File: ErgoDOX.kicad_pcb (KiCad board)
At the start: 2 copper layers, 182.8 x 158.9 mm, 113 parts, among them J1 USB, J2 3.5mm, J3 JMP, J4 JMP, J5 JMP, J6 JMP, SW1 SWITCH_PUSH, SW10 SWITCH_PUSH, SW11 SWITCH_PUSH, SW12 SWITCH_PUSH, SW13 SWITCH_PUSH, SW14 SWITCH_PUSH, SW15 SWITCH_PUSH, SW16 SWITCH_PUSH, SW17 SWITCH_PUSH, SW18 SWITCH_PUSH, SW19 SWITCH_PUSH, SW2 SWITCH_PUSH, SW20 SWITCH_PUSH, SW21 SWITCH_PUSH, SW22 SWITCH_PUSH, SW23 SWITCH_PUSH, SW24 SWITCH_PUSH, SW25 SWITCH_PUSH, SW26 SWITCH_PUSH, SW27 SWITCH_PUSH, SW28 SWITCH_PUSH, SW29 SWITCH_PUSH, SW3 SWITCH_PUSH, SW30 SWITCH_PUSH, SW31 SWITCH_PUSH, SW32 SWITCH_PUSH, SW33 SWITCH_PUSH, SW34 SWITCH_PUSH, SW35 SWITCH_PUSH, SW36 SWITCH_PUSH, SW37 SWITCH_PUSH, SW38 SWITCH_PUSH, SW39 SWITCH_PUSH, SW4 SWITCH_PUSH, SW40 SWITCH_PUSH, SW41 SWITCH_PUSH, SW42 SWITCH_PUSH, SW43 SWITCH_PUSH, SW44 SWITCH_PUSH, SW45 SWITCH_PUSH, SW46 SWITCH_PUSH, SW5 SWITCH_PUSH, SW6 SWITCH_PUSH, SW7 SWITCH_PUSH, SW8 SWITCH_PUSH, SW9 SWITCH_PUSH, U1 ProMicro

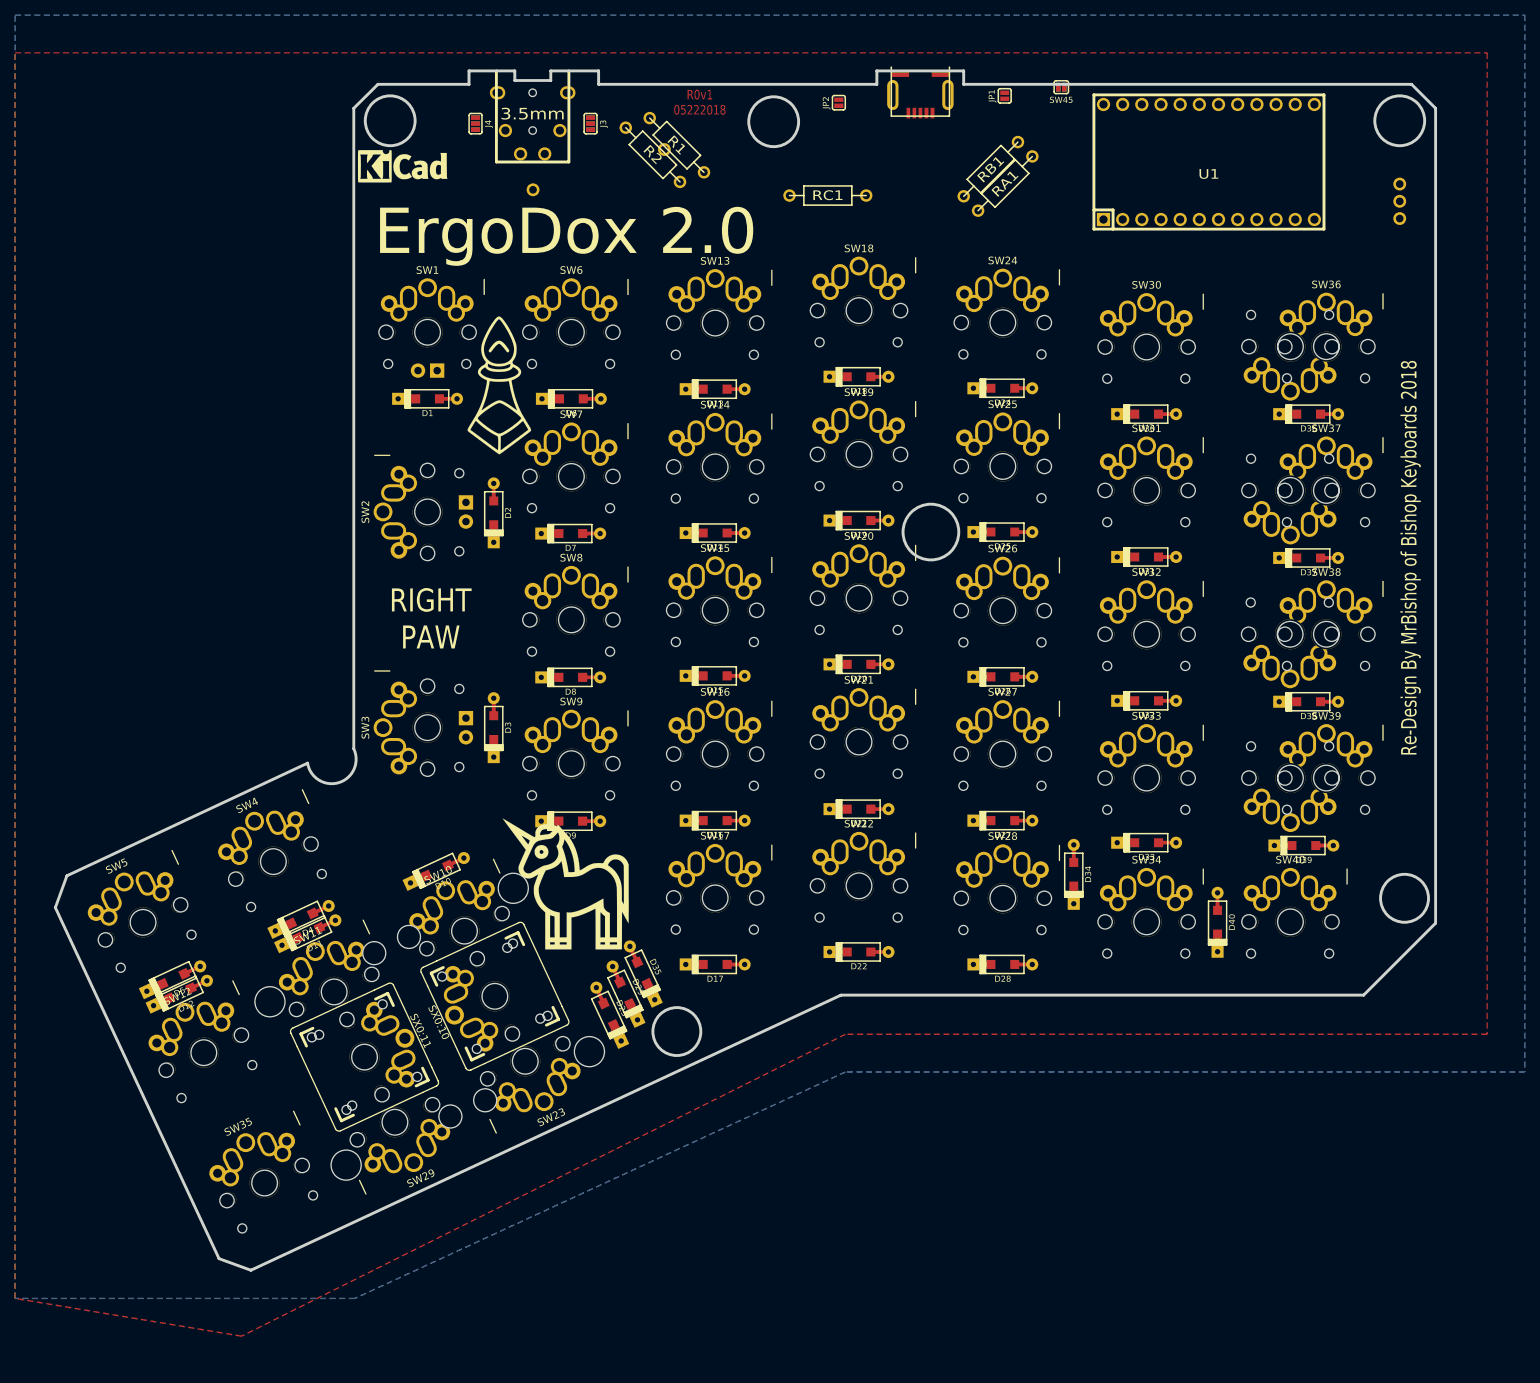
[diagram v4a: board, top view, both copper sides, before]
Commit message: fixed switch placement and begun traces
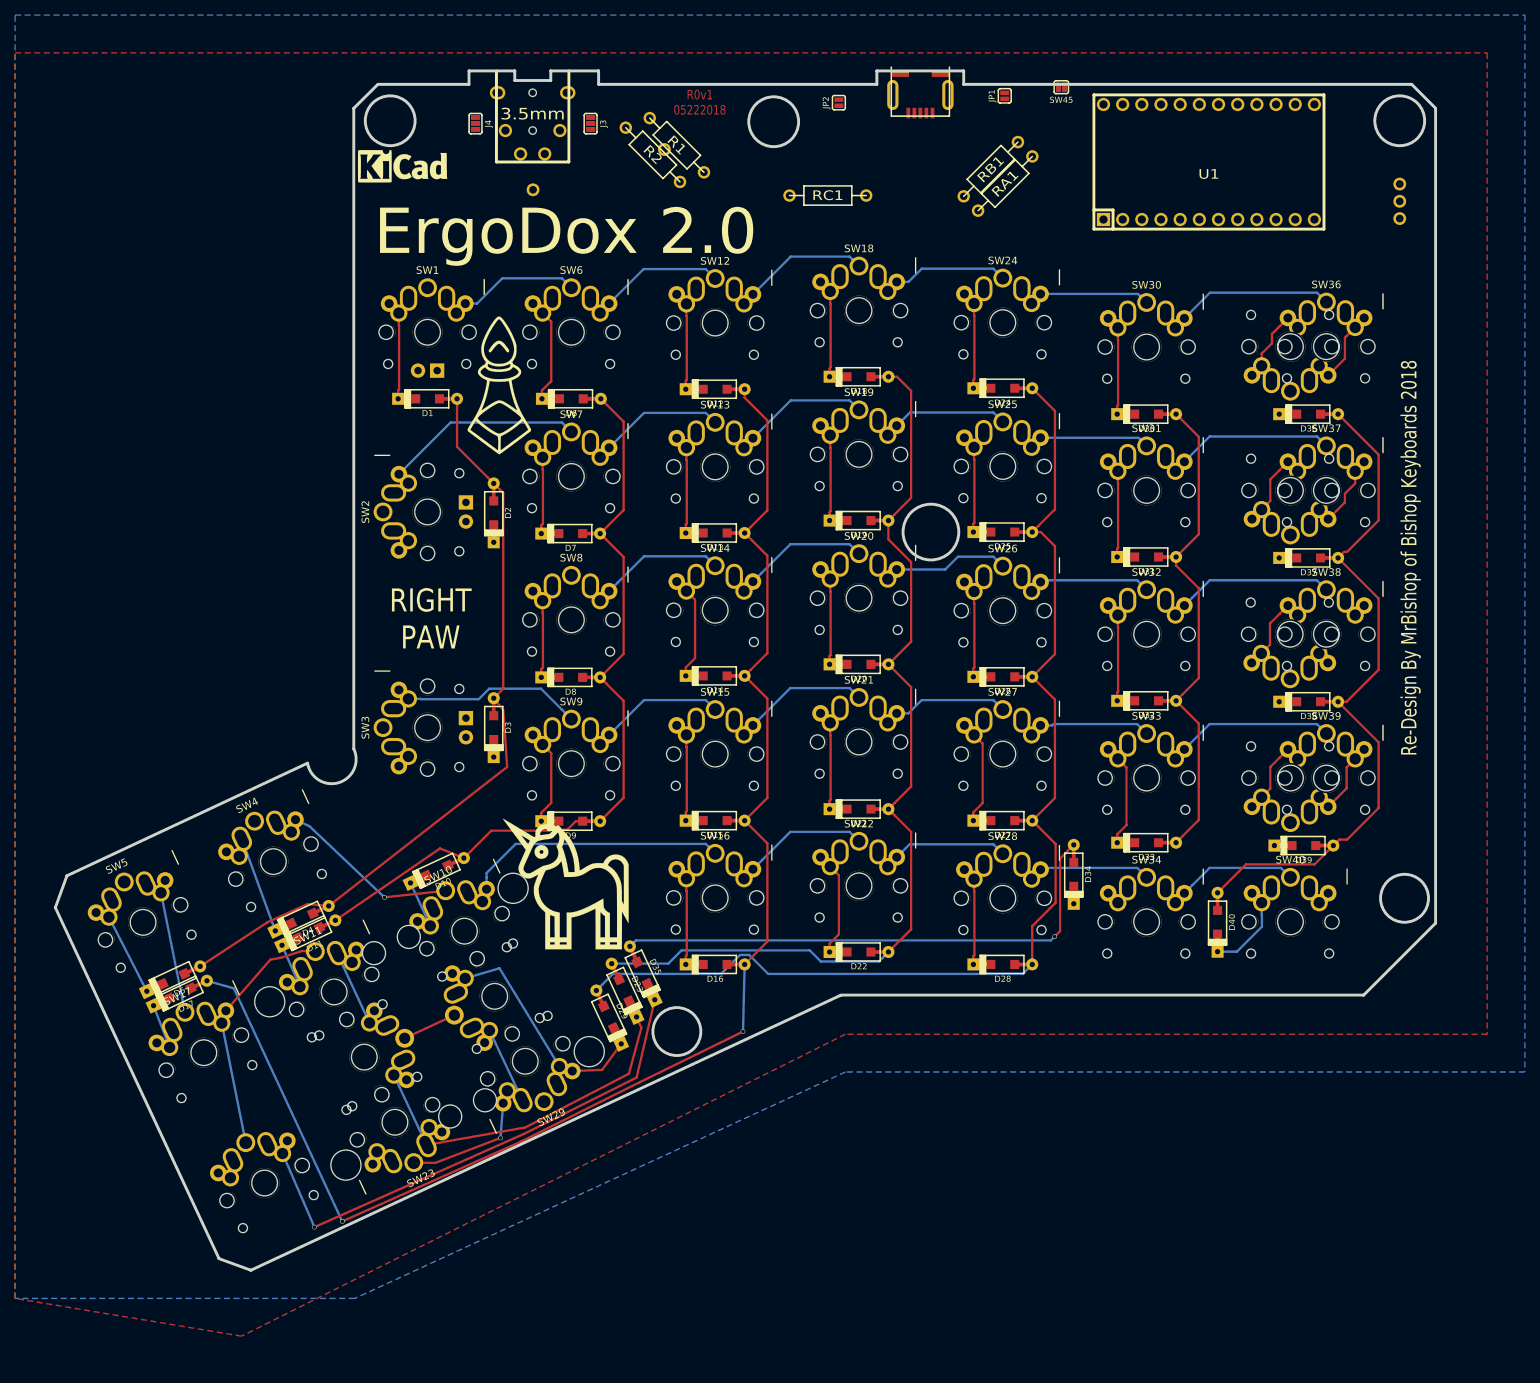
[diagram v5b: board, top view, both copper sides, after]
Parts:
- SW35: moved to B.Cu
- SX0:10: renamed from SX0:11; value SX0:2 -> SX0:3; moved to B.Cu
- SX0:11: renamed from SX0:10; value SX0:3 -> SX0:2; moved to B.Cu
- moved D29 3.84 mm to (96.4, 155.8)
- moved D23 3.77 mm to (98.4, 152.3)
- turned SX0:10 to 115 degrees
- turned SX0:11 to 295 degrees
- turned SW35 to 205 degrees
- renumbered D13 to D12, D14 to D13, D15 to D14, D16 to D15, D17 to D16, D12 to D17, SW13 to SW12, SW14 to SW13, SW15 to SW14, SW16 to SW15, SW17 to SW16, SW12 to SW17, SW29 to SW23, SW23 to SW29
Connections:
- SW12 pad 1: /ROW4 -> /ROW5
- SW13 pad 1: /ROW3 -> /ROW4
- SW14 pad 1: /ROW2 -> /ROW3
- SW15 pad 1: /ROW1 -> /ROW2
- SW16 pad 1: /ROW0 -> /ROW1
- SW17 pad 1: /ROW5 -> /ROW0
- SW23 pad 2: Net-(D29-Pad1) -> Net-(D23-Pad1)
- SW29 pad 2: Net-(D23-Pad1) -> Net-(D29-Pad1)
- SX0:10 pad 2: Net-(D29-Pad1) -> Net-(D23-Pad1)
- SX0:11 pad 2: Net-(D23-Pad1) -> Net-(D29-Pad1)
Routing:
- net /COL4: track 0.00 -> 191.6 mm, vias 0 -> 2
- net /COL2: track 0.00 -> 148.3 mm
- net /COL1: track 0.00 -> 134.2 mm, vias 0 -> 1
- net /COL3: track 0.00 -> 125.4 mm
- net /ROW1: track 0.00 -> 120.9 mm, vias 0 -> 1
- net /ROW4: track 0.00 -> 117.7 mm
- net /ROW2: track 0.00 -> 115.4 mm
- net /ROW5: track 0.00 -> 107.4 mm
- net /COL5: track 0.00 -> 101.6 mm
- net /COL6: track 0.00 -> 101.5 mm
- net /ROW0: track 0.00 -> 91.8 mm, vias 0 -> 1
- net /COL0: track 0.00 -> 90.1 mm
- net /ROW3: track 0.00 -> 83.8 mm
- net Net-(D35-Pad1): track 0.00 -> 68.3 mm, vias 0 -> 1
- net Net-(D23-Pad1): track 0.00 -> 46.8 mm
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
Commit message: initial traces complete
dont judge me on the thumb section i'm not crazy about how weird the wire traces are either.
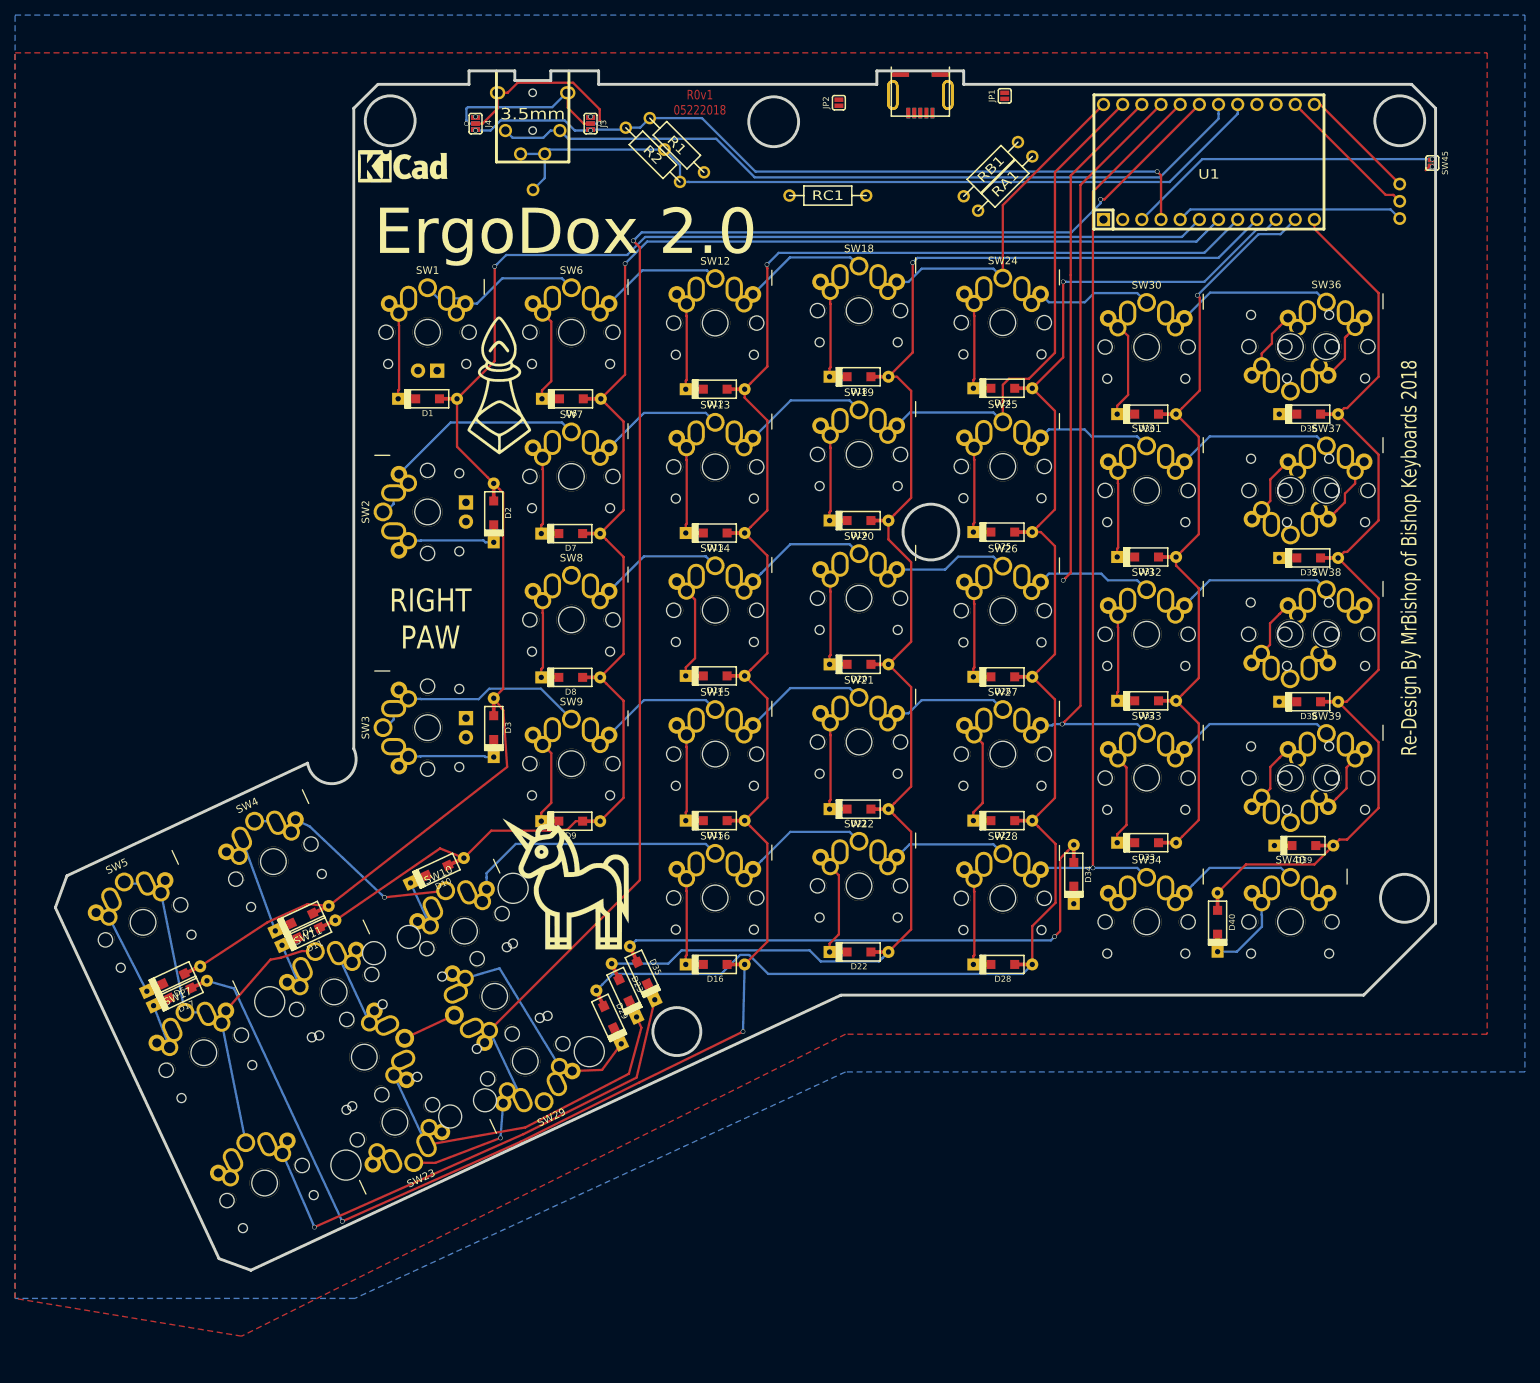
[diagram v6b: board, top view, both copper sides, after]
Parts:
- added J7: USB, BishopKicadConsolidated:USB_miniB_hirose_5S8, B.Cu at (137.7, 36.1)
- moved SW45 50.2 mm to (205.5, 42.7), turned to 270 degrees
- moved SW46 50.2 mm to (205.5, 42.7), turned to 270 degrees
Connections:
- J1 pad 2: (no net) -> /D-
- J1 pad 3: (no net) -> /D+
- J1 pad 4: (no net) -> /ID
- U1 pad 10: /COL4 -> /COL2
- U1 pad 11: /COL5 -> /COL1
- U1 pad 12: /COL6 -> /COL0
- U1 pad 6: /COL0 -> /COL6
- U1 pad 7: /COL1 -> /COL5
- U1 pad 8: /COL2 -> /COL4
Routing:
- net /ROW0: track 91.8 -> 302.4 mm, vias 1 -> 3
- net /COL6: track 101.5 -> 217.1 mm, vias 0 -> 1
- net /ROW1: track 120.9 -> 234.2 mm, vias 1 -> 2
- net /XTRADATA: track 0.00 -> 108.7 mm
- net /DATA: track 0.00 -> 102.9 mm
- net VCC: track 0.00 -> 101.7 mm, vias 0 -> 3
- net /COL5: track 101.6 -> 201.9 mm, vias 0 -> 1
- net /ROW2: track 115.4 -> 210.5 mm, vias 0 -> 1
- net /COL4: track 191.6 -> 274.2 mm, vias 2 -> 3
- net /ROW3: track 83.8 -> 151.8 mm, vias 0 -> 1
- net /COL3: track 125.4 -> 189.8 mm, vias 0 -> 1
- net /ROW4: track 117.7 -> 176.3 mm
- net /COL2: track 148.3 -> 195.7 mm, vias 0 -> 1
- net Net-(SW45-Pad1): track 0.00 -> 41.9 mm, vias 0 -> 1
- net /ROW5: track 107.4 -> 144.4 mm
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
